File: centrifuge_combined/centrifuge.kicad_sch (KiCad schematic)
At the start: 2 parts, among them J5 Conn_02x12_Odd_Even, J6 Conn_02x12_Odd_Even

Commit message: Almost finished releasable version
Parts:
- removed J6: Conn_02x12_Odd_Even, Connector_PinHeader_2.54mm:PinHeader_2x12_P2.54mm_Vertical, symbol Connector_Generic:Conn_02x12_Odd_Even
- added J504: Conn_02x05_Odd_Even, Connector_PinHeader_2.54mm:PinHeader_2x05_P2.54mm_Vertical, symbol Connector_Generic:Conn_02x05_Odd_Even
- added J518: Conn_02x03_Odd_Even, Connector_PinHeader_2.54mm:PinHeader_2x03_P2.54mm_Vertical, symbol Connector_Generic:Conn_02x03_Odd_Even
- added J519: Conn_02x02_Odd_Even, Connector_PinHeader_2.54mm:PinHeader_2x02_P2.54mm_Vertical, symbol Connector_Generic:Conn_02x02_Odd_Even
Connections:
- net +1V8_FPGA: no longer names the net of J5.8 (Pin_8)
- net +1V9_FPGA: no longer names the net of J5.10 (Pin_10)
- net +3V3A_FPGA: no longer names the net of J5.6 (Pin_6)
- net +3V3_FPGA: no longer names the net of J5.4 (Pin_4)
- net +5V_FPGA: no longer names the net of J5.2 (Pin_2)
- new net AUXIO1: J504.6 (Pin_6)
- new net AUXIO10: J518.4 (Pin_4)
- new net AUXIO11: J518.2 (Pin_2)
- new net AUXIO12: J504.4 (Pin_4)
- new net AUXIO13: J504.9 (Pin_9)
- new net AUXIO14: J504.10 (Pin_10)
- new net AUXIO15: J504.7 (Pin_7)
- new net AUXIO16: J504.8 (Pin_8)
- new net AUXIO17L: J518.1 (Pin_1)
- new net AUXIO2: J519.2 (Pin_2)
- new net AUXIO21: J504.1 (Pin_1)
- new net AUXIO23: J504.5 (Pin_5)
- new net AUXIO24: J504.3 (Pin_3)
- new net AUXIO3: J504.2 (Pin_2)
- new net AUXIO4: J519.4 (Pin_4)
- new net AUXIO5: J519.3 (Pin_3)
- new net AUXIO6: J519.1 (Pin_1)
- new net AUXIO7: J518.5 (Pin_5)
- new net AUXIO8: J518.3 (Pin_3)
- new net AUXIO9: J518.6 (Pin_6)

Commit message: Board appears ok
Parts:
- removed J5: Conn_02x12_Odd_Even, Connector_PinHeader_2.54mm:PinHeader_2x12_P2.54mm_Vertical, symbol Connector_Generic:Conn_02x12_Odd_Even
- added TP5: TestPoint, TestPoint:TestPoint_Keystone_5015_Micro-Minature, symbol Connector:TestPoint
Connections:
- net mcu_part/MCU_CLK: now also TP5.1

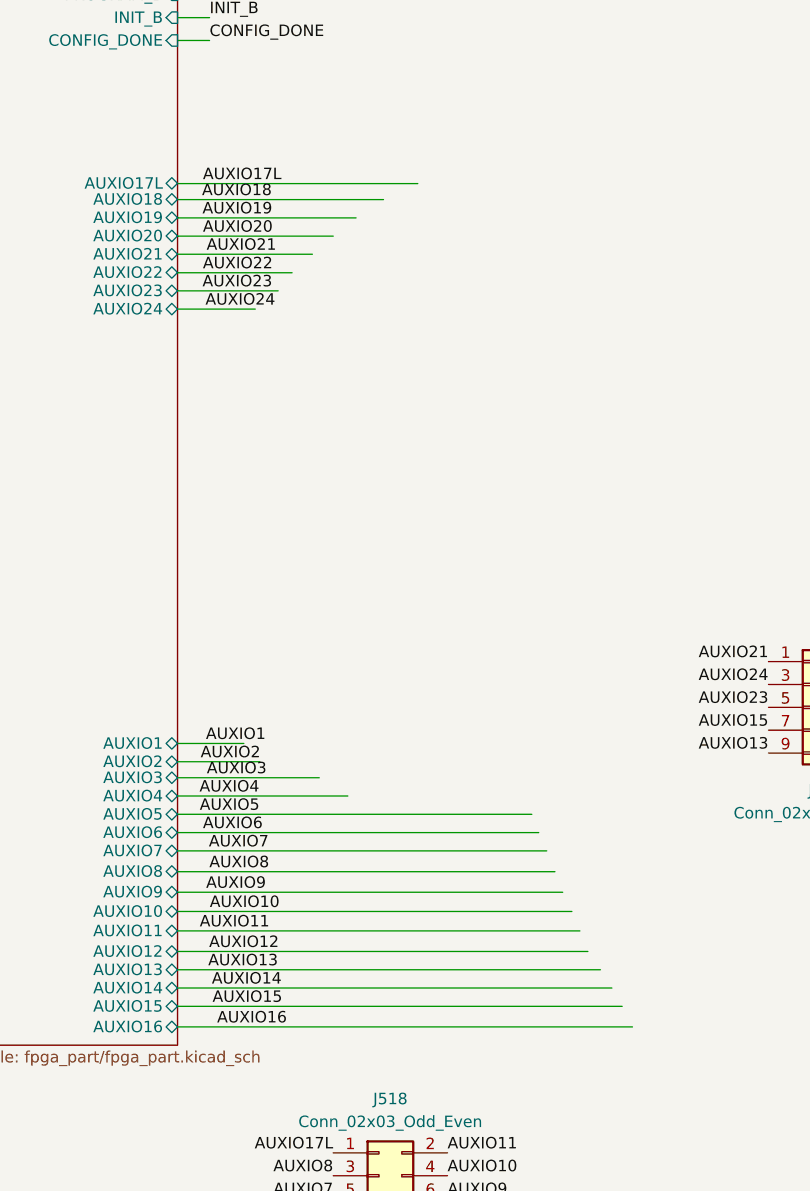
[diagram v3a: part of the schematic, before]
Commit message: Fixed missing footprints, added decoupling capacitors, adjusted board edges
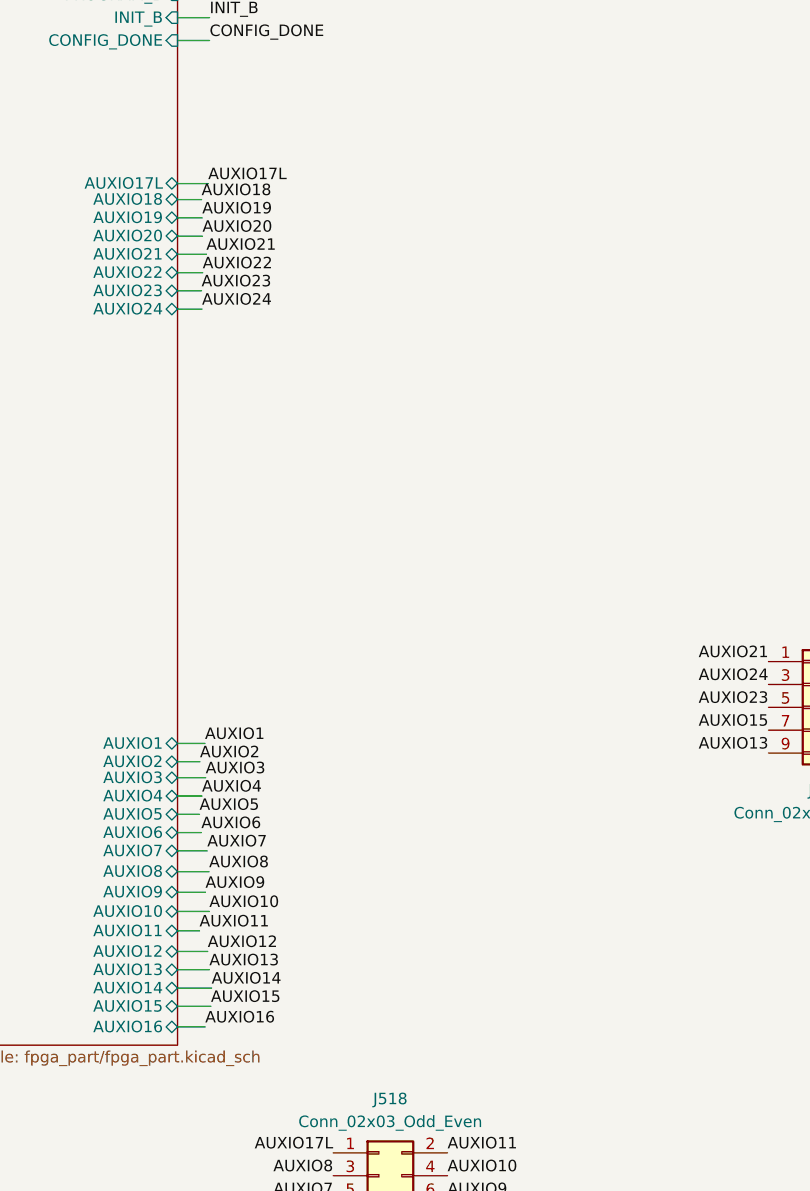
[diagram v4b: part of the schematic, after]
